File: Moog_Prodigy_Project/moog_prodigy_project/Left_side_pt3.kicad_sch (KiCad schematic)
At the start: 64 parts, among them SW7 SW_Slide_DPDT, SW9 SW_DPDT_x2, U1 MCP6562, U14C BF244A, U14E 4007, U2 AD8001AR, U3 MCP6562, U4 AD8001AR

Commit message: Final part of left side pt.2 29.03.2026
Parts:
- removed Vcc1, Vcc4, Vcc5, Vcc8, Vcc? (x4): -12V, symbol Power_supply:Vcc_reference
- removed Vcc2, Vcc3, Vcc6, Vcc7, Vcc? (x5): +12V, symbol Power_supply:Vcc_reference
- added VCC_positive_11, Vcc_11, Vcc_13, Vcc_14, Vcc_15, Vcc_16, Vcc_17, Vcc_18, Vcc_19: +12V, symbol Power_supply:Vcc_reference
- added Vcc_minus_10, Vcc_minus_11, Vcc_minus_13, Vcc_minus_14, Vcc_minus_15, Vcc_minus_7, Vcc_minus_8, Vcc_minus_9: -12V, symbol Power_supply:Vcc_reference
- R84: renamed from R3; value R -> 18KΩ
- gave numbers to parts that had none: 2
- renumbered CR1 to D1, CR2 to D2, SW7 to SW2, U5 to SW6, U2 to U11B, U3 to U12B, U1 to U13B
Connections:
- net at R103.1, U14E.1 (D): now also Vcc_15.
- net at U11B.7 (V+): now also Vcc_16.
- net at U4.4 (V-): now also Vcc_minus_13.
- net at U4.7 (V+): now also Vcc_19.
- net at U15.4 (V-): now also Vcc_minus_14.
- net at U15.7 (V+): now also Vcc_14.
- net at U11B.4 (V-): now also Vcc_minus_15.
- net at R81.1: now also Vcc_17.
- net at R88.1: now also Vcc_11.
- net at R92.3: now also Vcc_18.
- net at U14.7 (V+): now also Vcc_13.
- net at R96.1: now also VCC_positive_11.
- net at C24.2: now also Vcc_minus_11.
- net at R88.3: now also Vcc_minus_8.
- net at R92.1: now also Vcc_minus_9.
- net at U14.4 (V-): now also Vcc_minus_7.
- net at R83.2: now also Vcc_minus_10.
- net VISI KRAJ: now reaches SW2.3 (C)
- net VISI KRAJ: now also SW2.6 (C)
- net VISI PIN: now reaches SW6.8 (H)
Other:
- moved on the sheet: D1, D2, R77, R86, R87, R98, R99, SW6

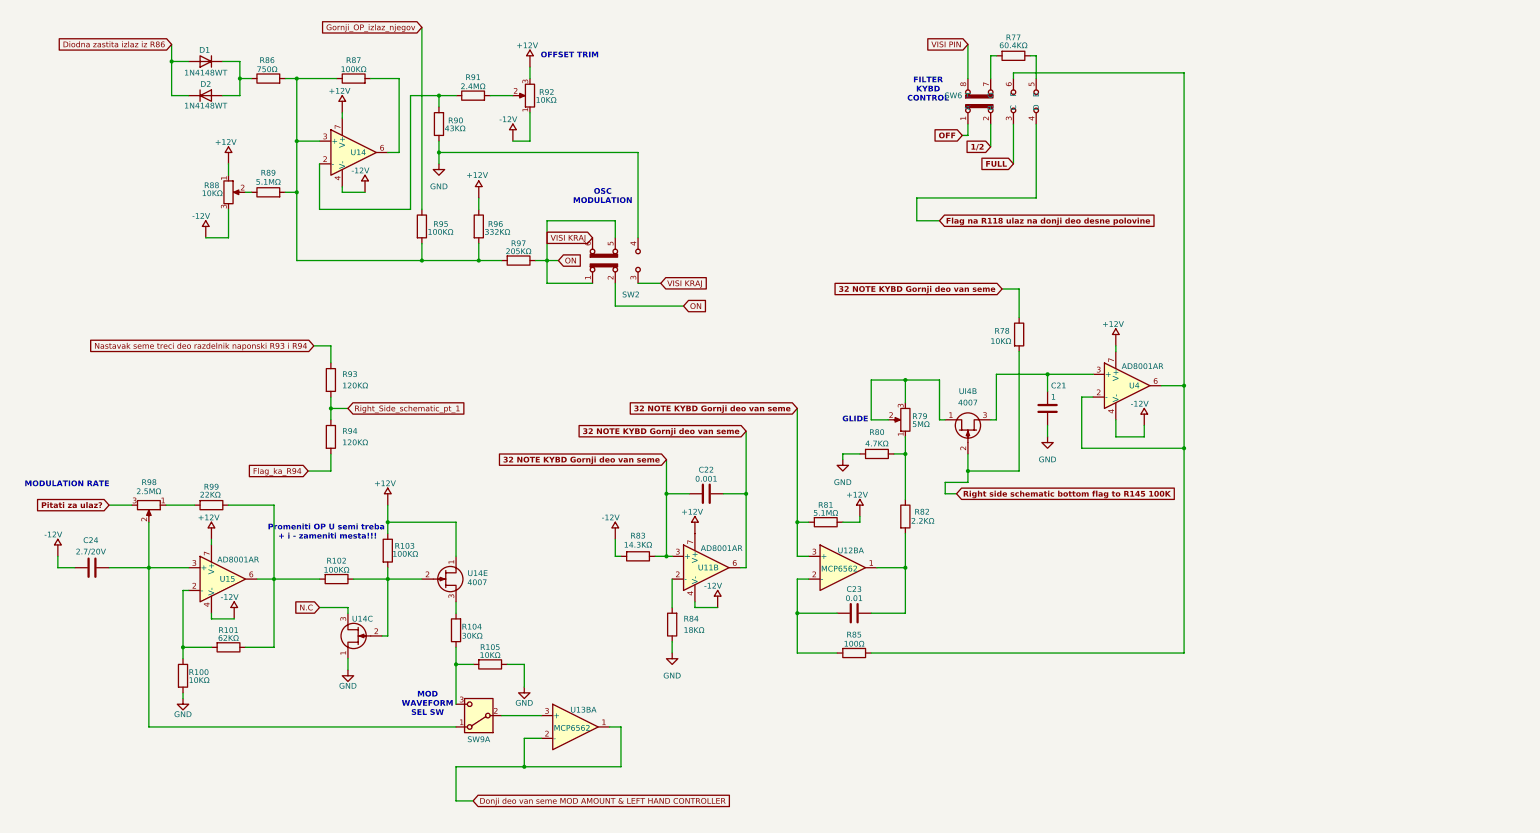
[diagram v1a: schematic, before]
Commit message: +12V & -12V fix flags
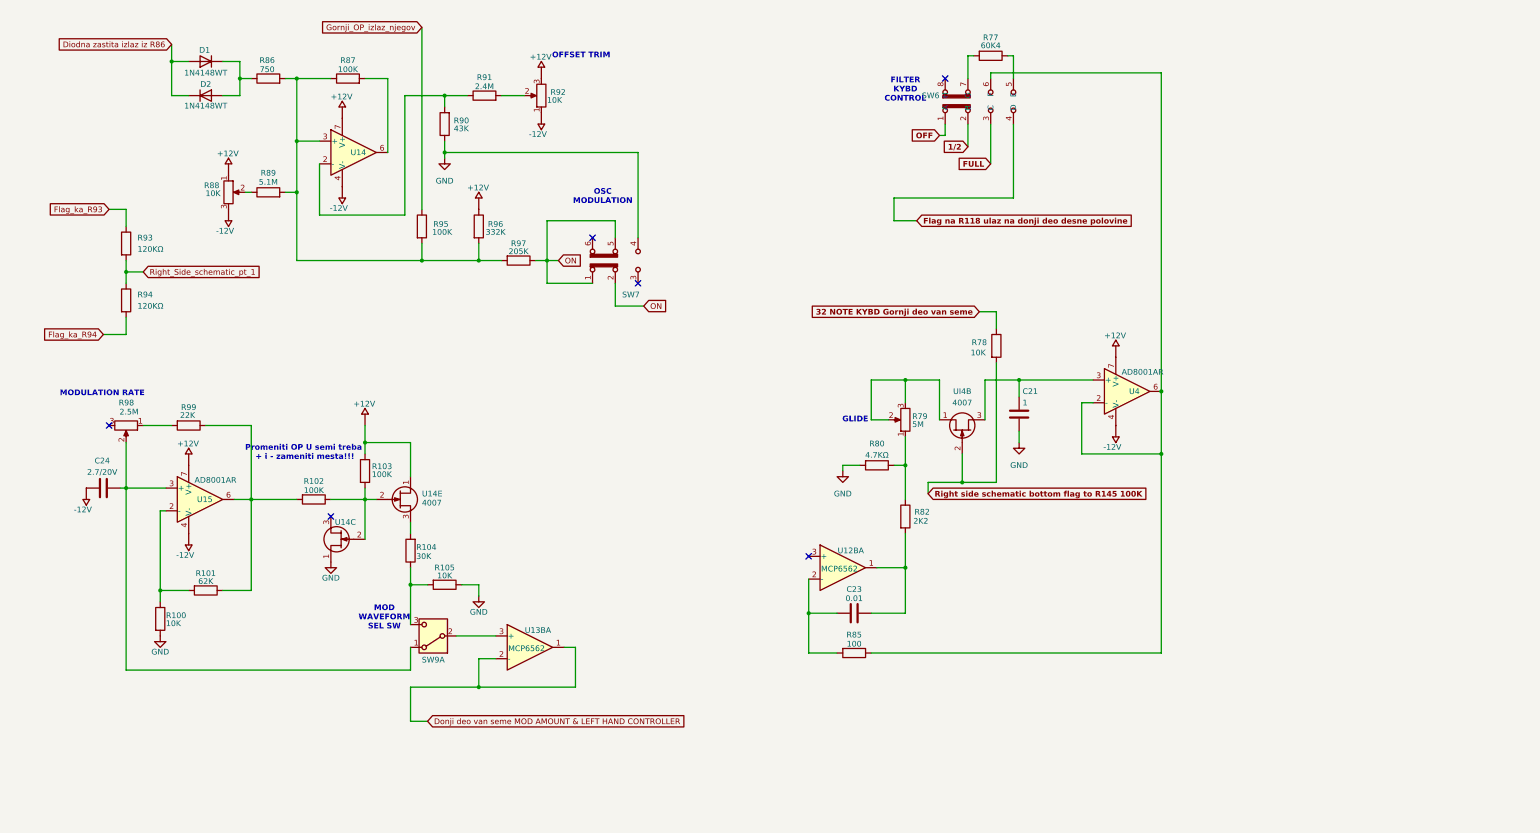
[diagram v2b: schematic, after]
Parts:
- removed C22: 0.001, symbol Device:C
- removed R81: 5.1MΩ, symbol Device:R
- removed R83: 14.3KΩ, symbol Device:R
- removed R84: 18KΩ, symbol Device:R
- removed U11B: AD8001AR, Package_SO:SOIC-8_3.9x4.9mm_P1.27mm, symbol Amplifier_Operational:AD8001AR
- removed VCC_positive_11, Vcc_11, Vcc_13, Vcc_14, Vcc_15, Vcc_16, Vcc_17, Vcc_18, Vcc_19: +12V, symbol Power_supply:Vcc_reference
- removed Vcc_minus_10, Vcc_minus_11, Vcc_minus_13, Vcc_minus_14, Vcc_minus_15, Vcc_minus_7, Vcc_minus_8, Vcc_minus_9: -12V, symbol Power_supply:Vcc_reference
- added Vcc__minus_17, Vcc__minus_18, Vcc__minus_19, Vcc__minus_20, Vcc__minus_21, Vcc__minus_3: -12V, symbol power:napajanje
- added Vcc__plus_24, Vcc__plus_25, Vcc__plus_26, Vcc__plus_27, Vcc__plus_28, Vcc__plus_29, Vcc__plus_4: +12V, symbol power:napajanje
- R100, R105, R78, R88, R92: value 10KΩ -> 10K
- R101: value 62KΩ -> 62K
- R102, R103, R87, R95: value 100KΩ -> 100K
- R104: value 30KΩ -> 30K
- R77: value 60.4KΩ -> 60K4
- R79: value 5MΩ -> 5M
- R82: value 2.2KΩ -> 2K2
- R85: value 100Ω -> 100
- R86: value 750Ω -> 750
- R89: value 5.1MΩ -> 5.1M
- R90: value 43KΩ -> 43K
- R91: value 2.4MΩ -> 2.4M
- R96: value 332KΩ -> 332K
- R97: value 205KΩ -> 205K
- R98: value 2.5MΩ -> 2.5M
- R99: value 22KΩ -> 22K
- renumbered SW2 to SW7
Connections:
- net 32 NOTE KYBD Gornji deo van seme: no longer U12B.3 (+)
- net at R103.1, U14E.1 (D): now also Vcc__plus_28.
- net at U14.4 (V-): now also Vcc__minus_18.
- net at U4.4 (V-): now also Vcc__minus_3.
- net at U4.7 (V+): now also Vcc__plus_4.
- net at U15.4 (V-): now also Vcc__minus_21.
- net at U15.7 (V+): now also Vcc__plus_29.
- net at R88.3: now also Vcc__minus_17.
- net at C24.2: now also Vcc__minus_20.
- net at R88.1: now also Vcc__plus_24.
- net at U14.7 (V+): now also Vcc__plus_25.
- net at R92.3: now also Vcc__plus_26.
- net at R96.1: now also Vcc__plus_27.
- net at R92.1: now also Vcc__minus_19.
- net N.C: no longer names the net of U14C.3 (S)
- net Nastavak seme treci deo razdelnik naponski R93 i R94 renamed Flag_ka_R93
- net Pitati za ulaz?: no longer names the net of R98.3
- net VISI KRAJ: no longer names the net of SW7.3 (C)
- net VISI KRAJ: no longer SW7.6 (C)
- net VISI PIN: no longer names the net of SW6.8 (H)
- no-connect marks 0 -> 6
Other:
- moved on the sheet: C21, C24, R100, R101, R102, R103, R104, R105, R77, R78, R80, R87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

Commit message: Imoprt LF393 & Sortiranje fleg-ova 07.04.2026
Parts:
- removed D1, D2: 1N4148WT, Diode_SMD:D_SOD-523, symbol Diode:1N4148WT
- removed R78: 10K, symbol Device:R
- added CR1, CR2: 1N4148, Diode_THT:D_DO-35_SOD27_P7.62mm_Horizontal, symbol Diode:1N4148
- C21: value 1 -> 1000n
- C23: value 0.01 -> 10n
- R93, R94: value 120KΩ -> 120K
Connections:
- net Gornji_OP_izlaz_njegov is gone; now on an unnamed net: R95.1
- net at R86.1: now also CR1.1 (K), CR2.2 (A)
- net Right_Side_schematic_pt_1 renamed Pocetak_Babicevog_dela_Leader
- new net Ulaz_na_diodnu_zastitu: CR1.2 (A), CR2.1 (K)
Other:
- moved on the sheet: C21, C23, C24, R100, R101, R102, R103, R104, R105, R77, R79, R80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

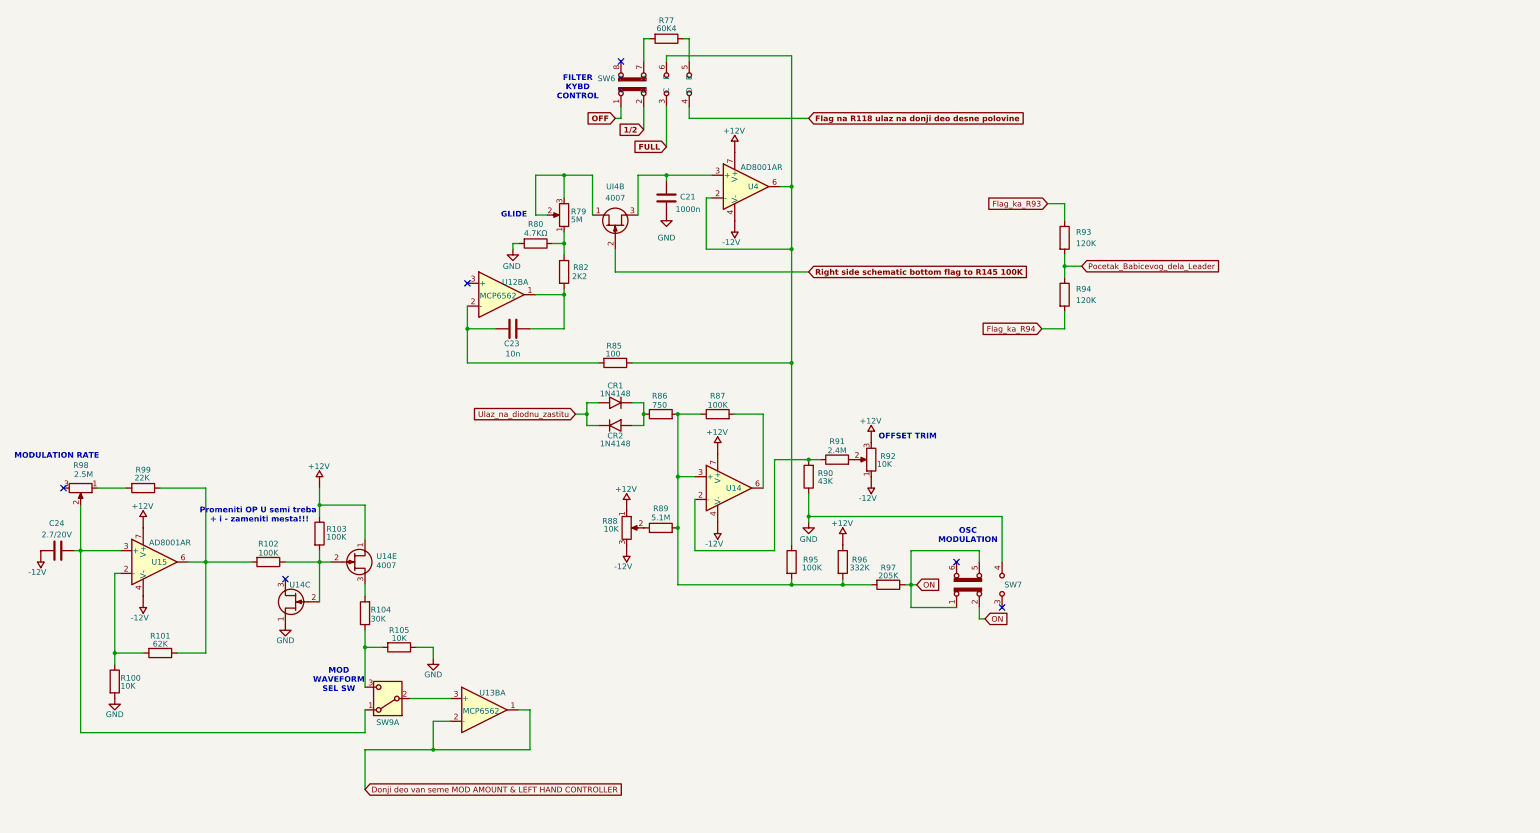
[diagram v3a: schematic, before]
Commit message: Dodavanje evropskih komponenti u semu 11.04.2026
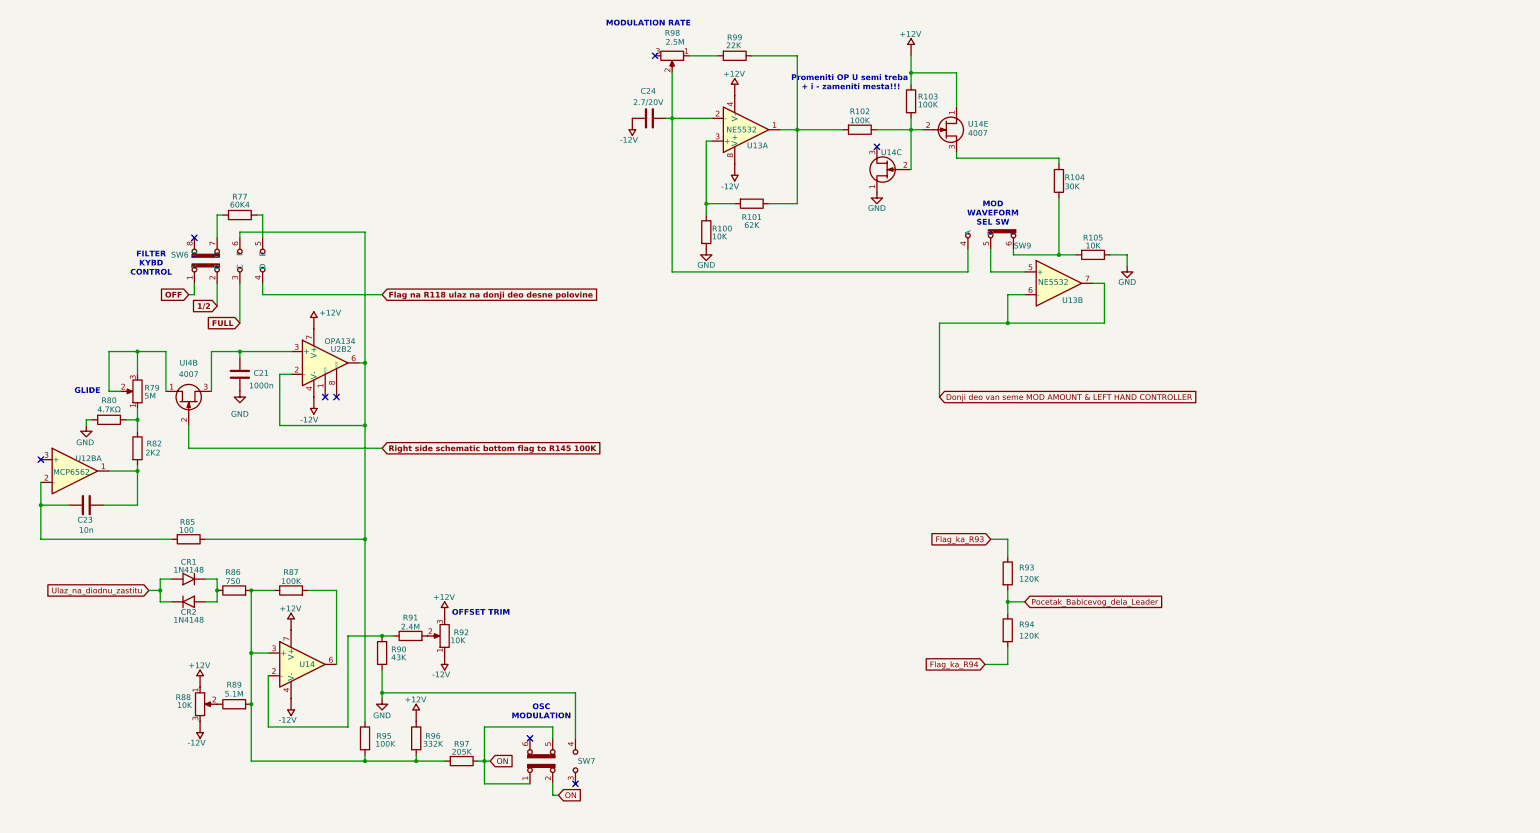
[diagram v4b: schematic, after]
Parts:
- removed SW9: SW_DPDT_x2, symbol Switch:SW_DPDT_x2
- removed U13B: MCP6562, symbol Comparator:MCP6562
- removed U15, U4: AD8001AR, Package_SO:SOIC-8_3.9x4.9mm_P1.27mm, symbol Amplifier_Operational:AD8001AR
- removed Vcc__minus_21, Vcc__minus_3: -12V, symbol power:napajanje
- removed Vcc__plus_29, Vcc__plus_4: +12V, symbol power:napajanje
- added SW9: ~, symbol Switch:DPDT2
- added U13, U2: NE5532, symbol Amplifier_Operational:NE5532
- added U2B2: OPA134, symbol Amplifier_Operational:OPA134
- added Vcc__minus_15, Vcc__minus_9: -12V, symbol power:napajanje
- added Vcc__plus_13, Vcc__plus_17: +12V, symbol power:napajanje
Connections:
- net Donji deo van seme MOD AMOUNT & LEFT HAND CONTROLLER: now also U13.6 (-), U13.7
- net at C21.2, UI4B.3 (S): now also U2B2.3 (+)
- net at R85.1, R95.1, SW6.6 (F): now also U2B2.2 (-), U2B2.6
- net at R101.1, R102.2, R99.1: now also U13.1
- net at R100.1, R101.2: now also U13.3 (+)
- net at C24.1, R98.2: now also SW9.4 (A), U13.2 (-)
- net at R104.1, R105.2: now also SW9.6 (C)
- new net: U2B2.7 (V+), Vcc__plus_17.
- new net: SW9.5 (B), U13.5 (+)
- new net: U2B2.4 (V-), Vcc__minus_9.
- new net: U2.4 (V-), Vcc__plus_13.
- new net: U2.8 (V+), Vcc__minus_15.
- no-connect marks 6 -> 8
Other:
- moved on the sheet: C21, C23, C24, CR1, CR2, R100, R101, R102, R103, R104, R105, R77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

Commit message: LM393BIPWR izmena, dodavanje spoljnih delova pt.2, 12.04.2026
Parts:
- added PI-2, PI-3, PI-4: Conn_02x01, symbol Connector_Generic:Conn_02x01
- added R29: 10K, symbol Device:R_Potentiometer
- renumbered U14E to U14E?
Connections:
- net GND: now also PI-2.1 (Pin_1)
- net ON: no longer SW7.2 (B)
- net Donji deo van seme MOD AMOUNT & LEFT HAND CONTROLLER: no longer names the net of U13.6 (-), U13.7
- net Donji deo van seme MOD AMOUNT & LEFT HAND CONTROLLER: now also PI-3.1 (Pin_1)
- new net: PI-3.2 (Pin_2), R29.1
- new net: PI-2.2 (Pin_2), R29.3
- new net: PI-4.2 (Pin_2), R29.2
- new net SW8 PREKIDAC KOD BABICA FILTER MODE: PI-4.1 (Pin_1), SW7.2 (B)
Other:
- note added: "LEFT HAND CONTROLLER"
- note added: "MOD AMOUNT"
- note removed: "Promeniti OP U semi treba + i - zameniti mesta!!!"
- moved on the sheet: C21, C23, C24, CR1, CR2, R100, R101, R102, R103, R104, R105, R77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
